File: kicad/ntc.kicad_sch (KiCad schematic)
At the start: 24 parts, among them J1 AudioJack2_SwitchT, J2 AudioJack2_SwitchT, J3 Conn_01x03, J4 AudioJack2_SwitchT, J5 AudioJack2_SwitchT, J6 AudioJack2_SwitchT, J7 AudioJack2_SwitchT, Q1 DMN61D9UWQ-13, Q2 DMP31D0U-7

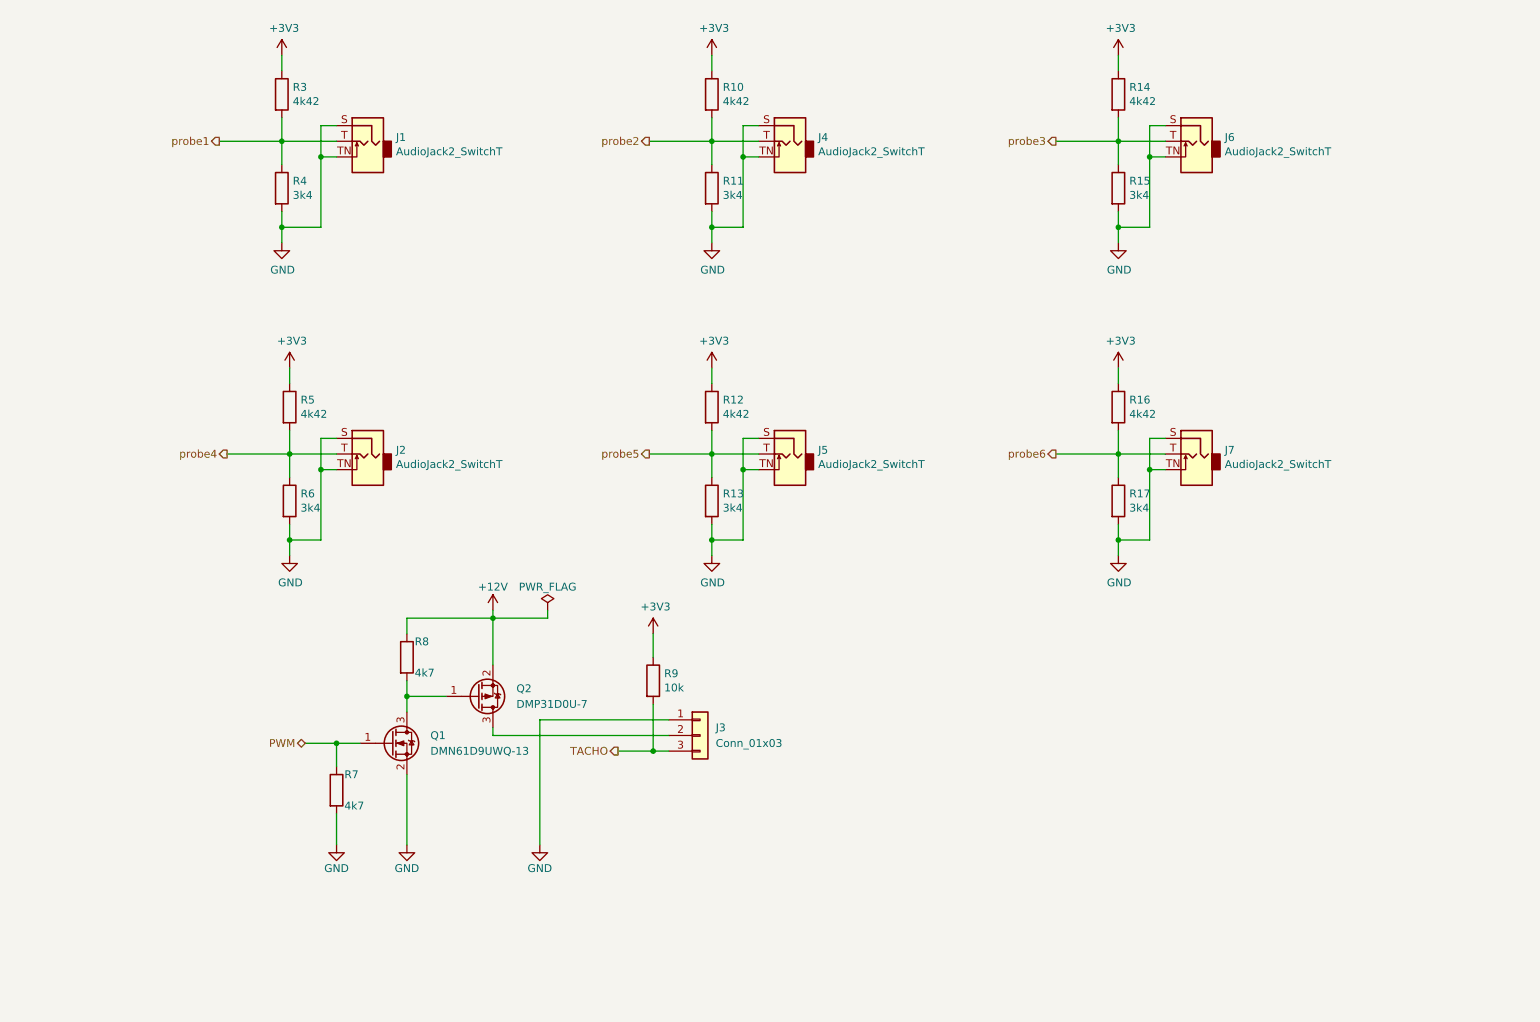
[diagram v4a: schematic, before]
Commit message: add all digikeys numbers to schematic
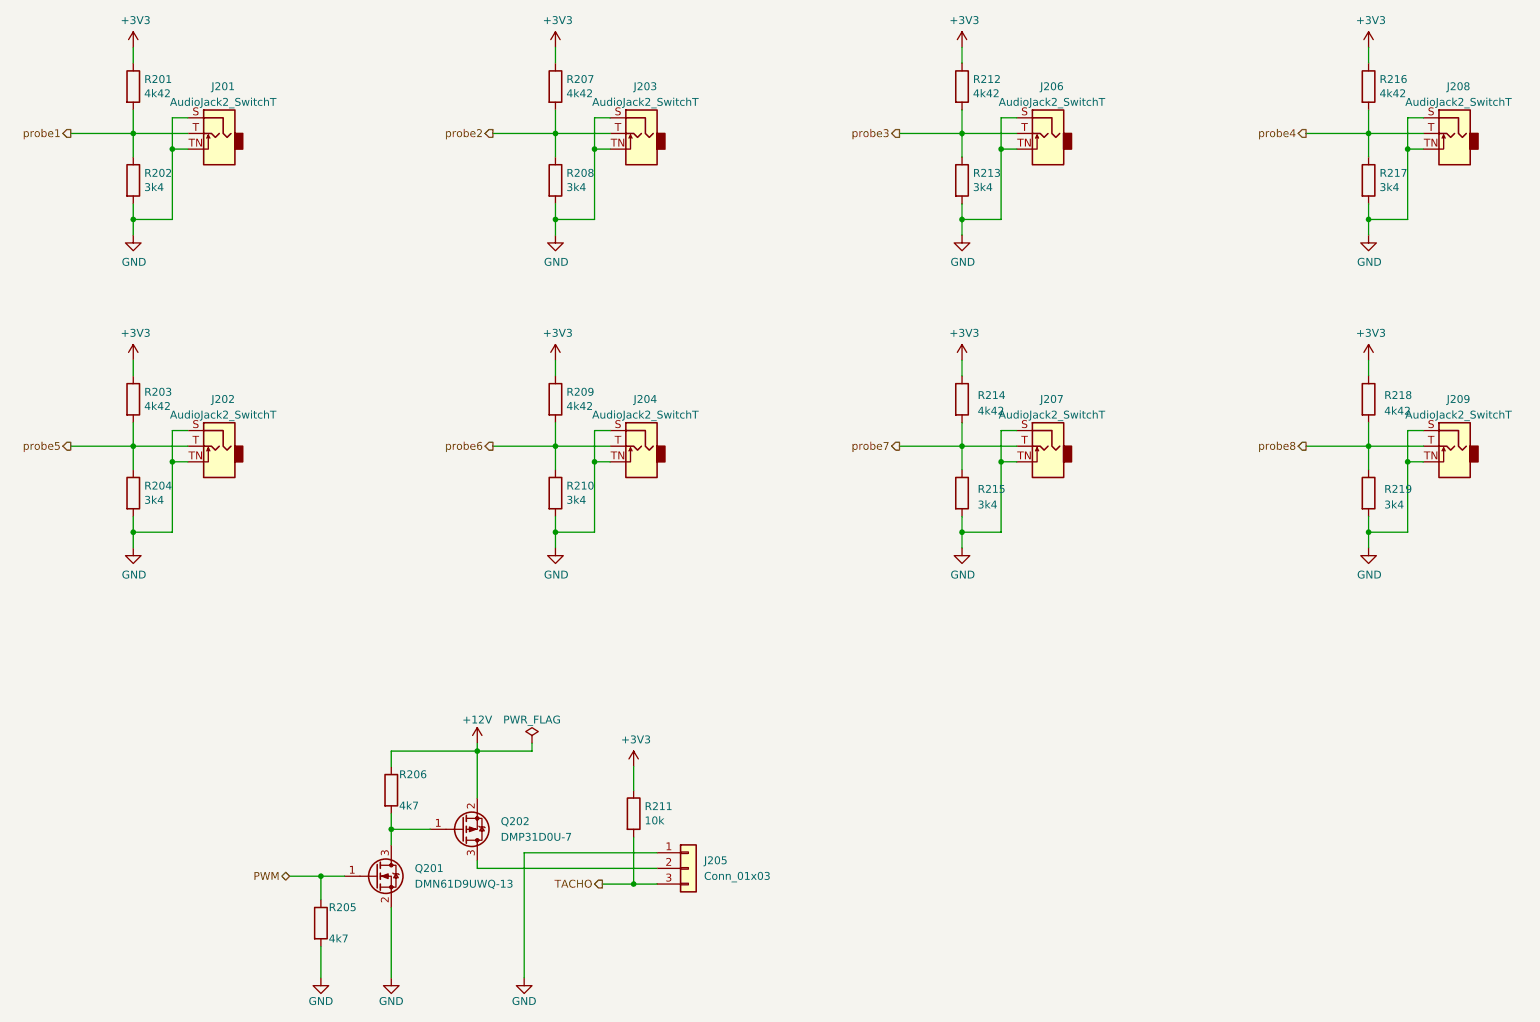
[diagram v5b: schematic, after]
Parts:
- removed J1, J2, J4, J5, J6, J7: AudioJack2_SwitchT, mylib_connector:MJ-2523, symbol Connector:AudioJack2_SwitchT
- added J201, J202, J203, J204, J206, J207, J208, J209: AudioJack2_SwitchT, mylib_connector:MJ-2523, symbol Connector_Audio:AudioJack2_SwitchT
- added R216, R218: 4k42, Resistor_SMD:R_0603_1608Metric, symbol Device:R
- added R217, R219: 3k4, Resistor_SMD:R_0603_1608Metric, symbol Device:R
- J205: renamed from J3; footprint z_connector:Molex_KK-254_AE-6410-03A_1x03_P2.54mm_Vertical -> mylib_connector:Molex_KK-254_AE-6410-03A_1x03_P2.54mm_Vertical
- renumbered Q1 to Q201, Q2 to Q202, R3 to R201, R4 to R202, R5 to R203, R6 to R204, R7 to R205, R8 to R206, R10 to R207, R11 to R208, R12 to R209, R13 to R210, R9 to R211, R14 to R212, R15 to R213, R16 to R214, R17 to R215
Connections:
- net +3V3: now also R216.1, R218.1
- net GND: now also J201.S, J201.TN, J202.S, J202.TN, J203.S, J203.TN, J204.S, J204.TN, J206.S, J206.TN, J207.S, J207.TN, J208.S, J208.TN, J209.S, J209.TN, R217.2, R219.2
- net probe1: now also J201.T
- net probe2: now also J203.T
- net probe3: now also J206.T
- net probe4: now also J208.T, R216.2, R217.1; no longer R203.2, R204.1
- net probe5: now also R203.2, R204.1, J202.T; no longer R209.2, R210.1
- net probe6: now also R209.2, R210.1, J204.T; no longer R214.2, R215.1
- new net probe7: J207.T, R214.2, R215.1
- new net probe8: J209.T, R218.2, R219.1
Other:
- moved on the sheet: J205, Q201, Q202, R201, R202, R203, R204, R205, R206, R207, R208, R209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

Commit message: wip
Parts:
- removed J207, J209: AudioJack2_SwitchT, mylib_connector:MJ-2523, symbol Connector_Audio:AudioJack2_SwitchT
- removed R214, R218: 4k42, Resistor_SMD:R_0603_1608Metric, symbol Device:R
- removed R215, R219: 3k4, Resistor_SMD:R_0603_1608Metric, symbol Device:R
- renumbered J203 to J202, J206 to J203, J202 to J204, J204 to J205, J208 to J206, J205 to J207, Q202 to Q201, Q201 to Q202, R207 to R202, R212 to R203, R202 to R204, R208 to R205, R213 to R206, R203 to R207, R209 to R208, R216 to R209, R204 to R210, R210 to R211, R217 to R212, R206 to R213, R211 to R214, R205 to R215
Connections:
- net probe1: now also J202.T, R202.2, R205.1; no longer J201.T, R201.2, R204.1
- net probe2: now also J203.T, R203.2, R206.1; no longer J202.T, R202.2, R205.1
- net probe3: now also J204.T, R207.2, R210.1; no longer J203.T, R203.2, R206.1
- net probe4: now also J205.T, R208.2, R211.1; no longer J206.T, R209.2, R212.1
- net probe5: now also J206.T, R209.2, R212.1; no longer J204.T, R207.2, R210.1
- net probe6: no longer J205.T, R208.2, R211.1
- new net probe0: J201.T, R201.2, R204.1
- no-connect marks 0 -> 2
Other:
- moved on the sheet: J204, J205, J206, J207, Q201, Q202, R207, R208, R209, R210, R211, R212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

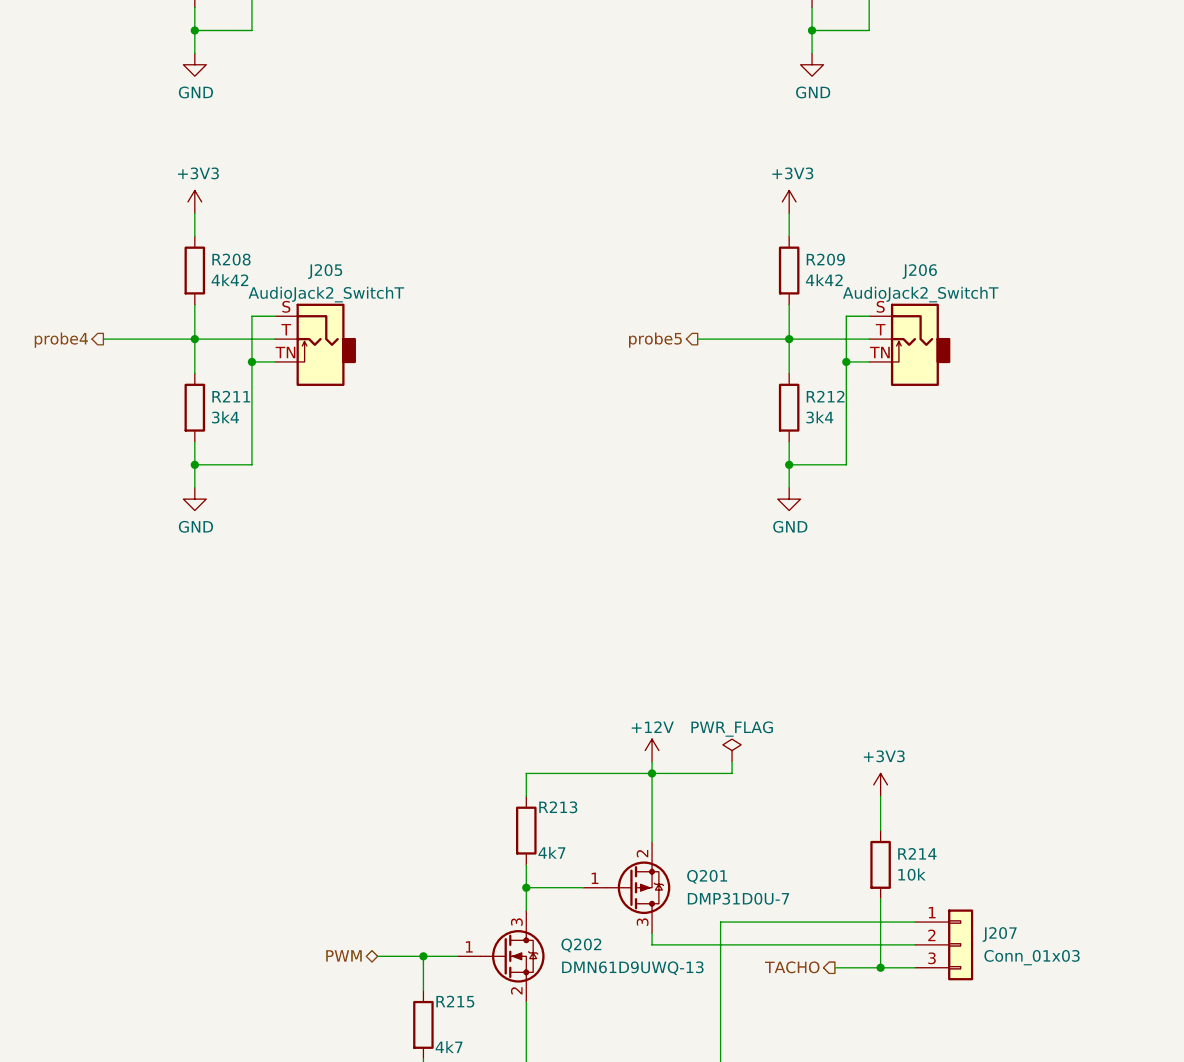
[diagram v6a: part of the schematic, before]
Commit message: add nrf52840 board
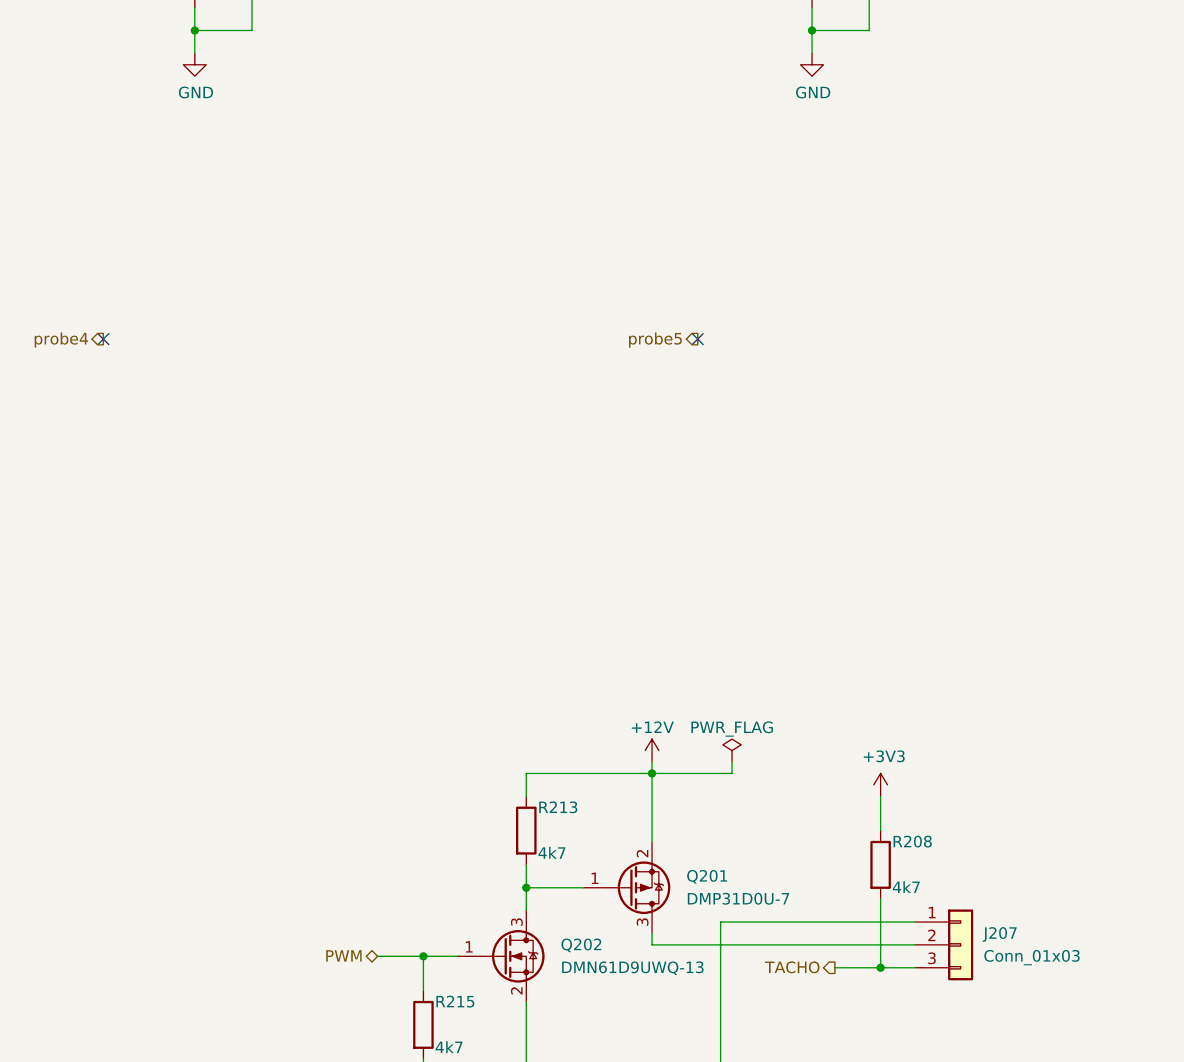
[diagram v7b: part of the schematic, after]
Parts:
- removed J205, J206: AudioJack2_SwitchT, mylib_connector:MJ-2523, symbol Connector_Audio:AudioJack2_SwitchT
- removed R209: 4k42, Resistor_SMD:R_0603_1608Metric, symbol Device:R
- removed R211, R212: 3k4, Resistor_SMD:R_0603_1608Metric, symbol Device:R
- removed R214: 10k, Resistor_SMD:R_0603_1608Metric, symbol Device:R
- R208: value 4k42 -> 4k7; Digikey RMCF0603FT4K42CT-ND -> 311-4.70KHRCT-ND
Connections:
- net TACHO: now also R208.2
- net probe4: no longer R208.2
- no-connect marks 2 -> 4

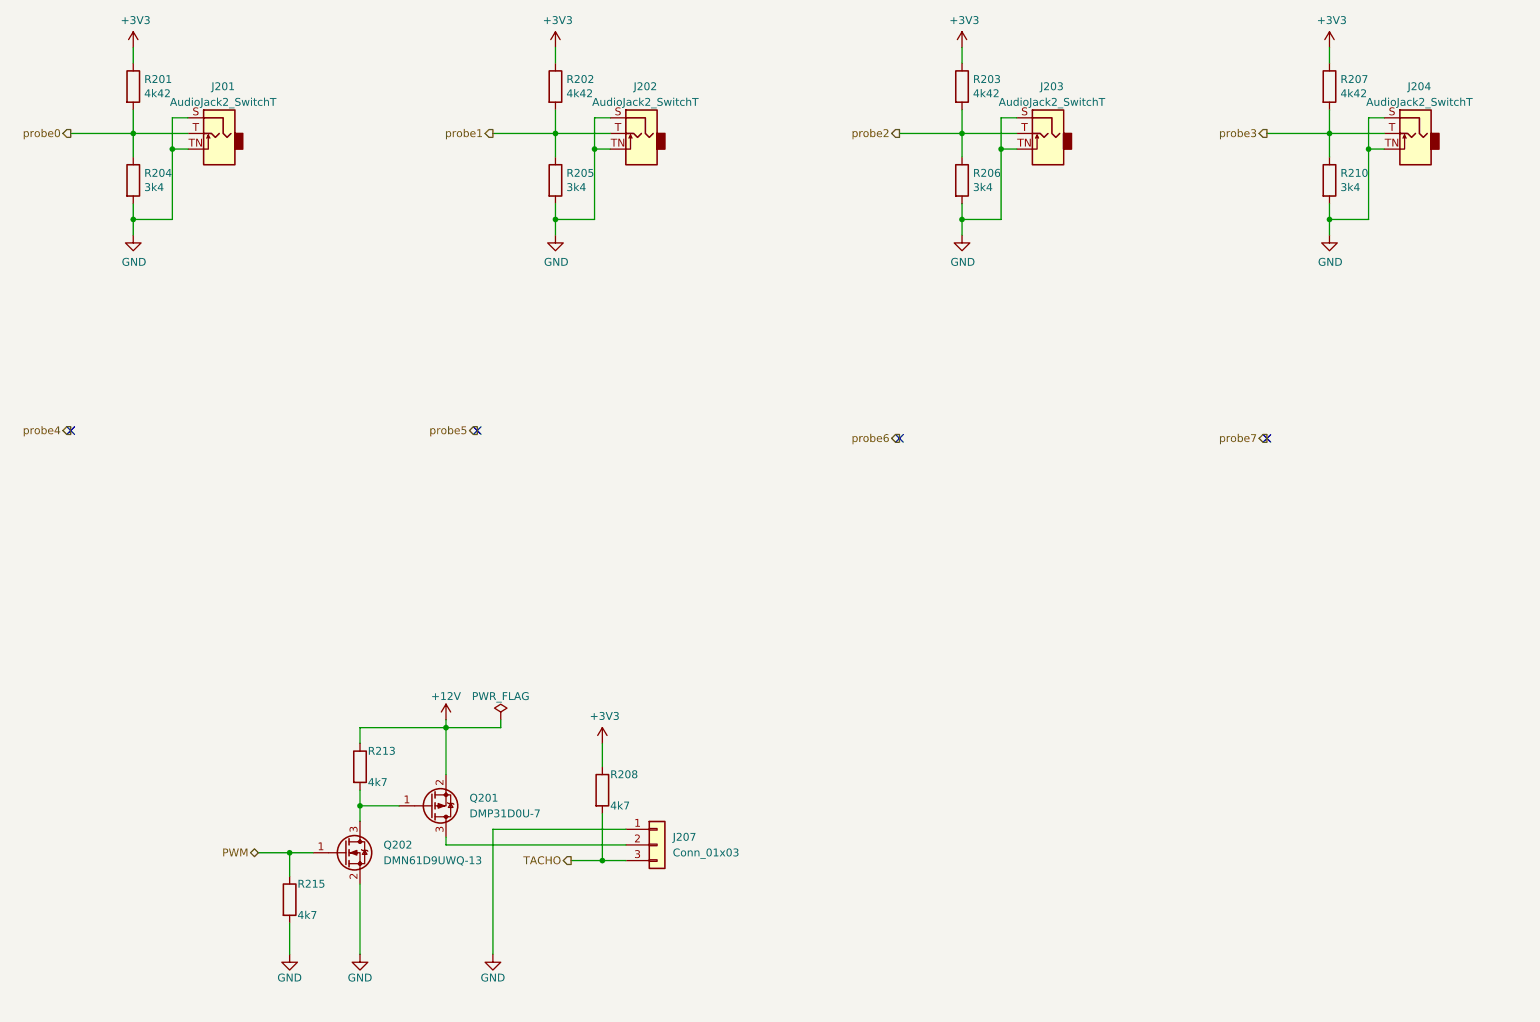
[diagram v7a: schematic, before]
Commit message: rework board
add nrf 7002
add oled display
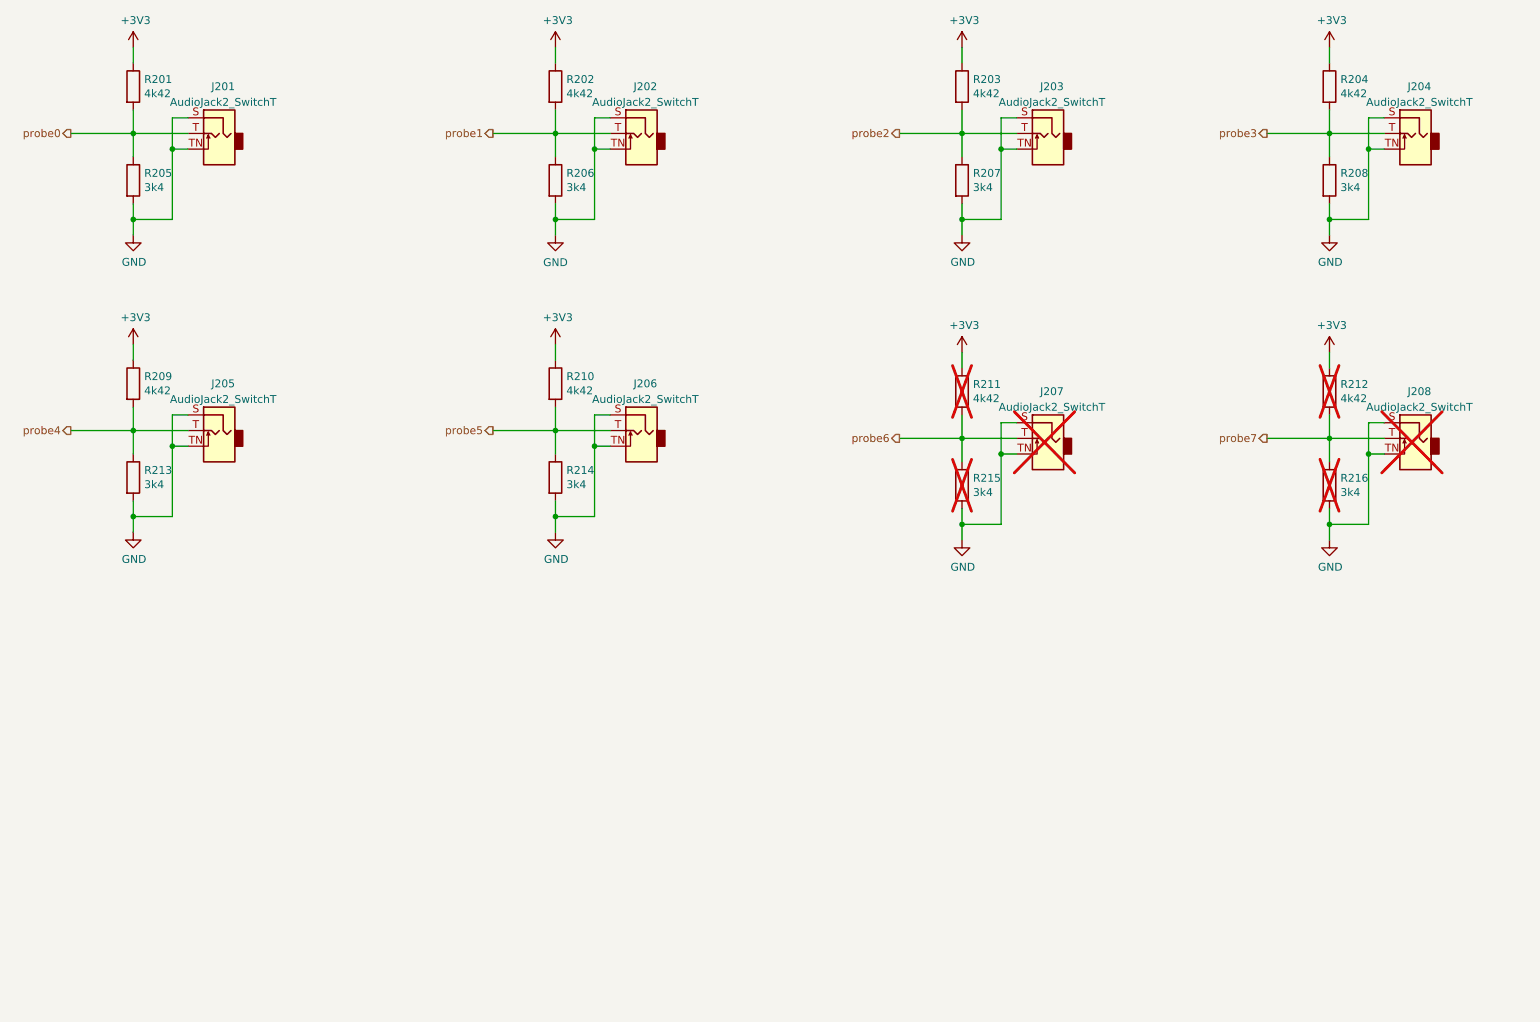
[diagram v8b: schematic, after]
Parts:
- removed J207: Conn_01x03, mylib_connector:Molex_KK-254_AE-6410-03A_1x03_P2.54mm_Vertical, symbol Connector_Generic:Conn_01x03
- removed Q201: DMP31D0U-7, Package_TO_SOT_SMD:SOT-23, symbol Device:Q_PMOS_GSD
- removed Q202: DMN61D9UWQ-13, Package_TO_SOT_SMD:SOT-323_SC-70, symbol Device:Q_NMOS_GSD
- removed R208: 4k7, Resistor_SMD:R_0603_1608Metric, symbol Device:R
- added J205, J206, J207, J208: AudioJack2_SwitchT, mylib_connector:MJ-2523, symbol Connector_Audio:AudioJack2_SwitchT
- added R209, R210, R211, R212: 4k42, Resistor_SMD:R_0603_1608Metric, symbol Device:R
- added R214, R216: 3k4, Resistor_SMD:R_0603_1608Metric, symbol Device:R
- R213: value 4k7 -> 3k4; Digikey 311-4.70KHRCT-ND -> 311-3.40KHRCT-ND
- R215: value 4k7 -> 3k4; Digikey 311-4.70KHRCT-ND -> 311-3.40KHRCT-ND; now not fitted; now left out of the parts list
- renumbered R207 to R204, R204 to R205, R205 to R206, R206 to R207, R210 to R208
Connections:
- net +12V is gone; now on net probe4: R213.1
- net PWM is gone; now on net probe6: R215.1
- net +3V3: now also R209.1, R210.1, R211.1, R212.1
- net GND: now also R213.2, J205.S, J205.TN, J206.S, J206.TN, J207.S, J207.TN, J208.S, J208.TN, R214.2, R216.2
- net probe4: now also J205.T, R209.2
- net probe5: now also J206.T, R210.2, R214.1
- net probe6: now also J207.T, R211.2
- net probe7: now also J208.T, R212.2, R216.1
- no-connect marks 4 -> 0
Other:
- title: (none) -> Firewaterburn
